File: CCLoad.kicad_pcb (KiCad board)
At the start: 2 copper layers, 100 x 50 mm, 37 parts, among them J101 BANANA, J102 BANANA, J103 MOLEX, J104 BTS117, J105 SCREW_TERMINAL, J106 MOLEX, SW101 SW_DP3T, U101 HT7533-1 (3V3), U102 CJ431, U103 MCP6002-xP

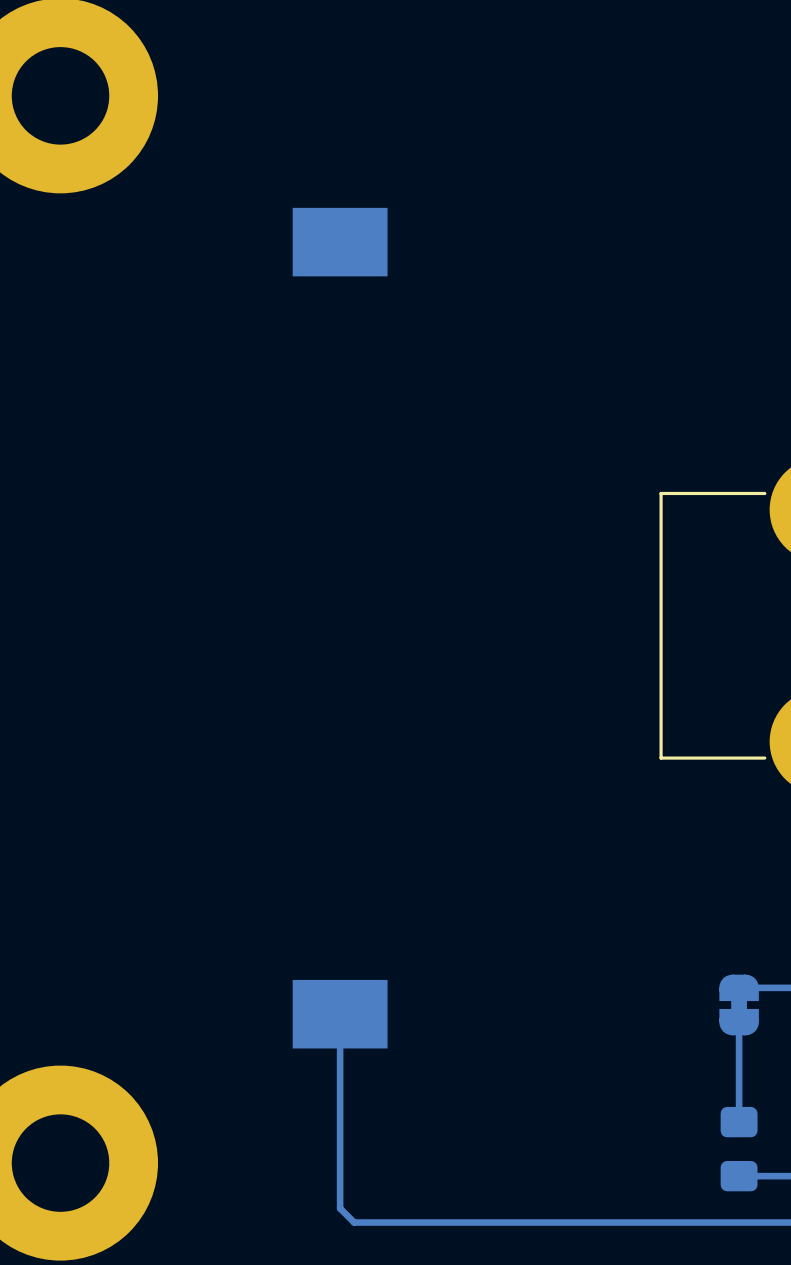
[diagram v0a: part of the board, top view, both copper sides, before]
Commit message: increases banana mounting hole to 4.5mm
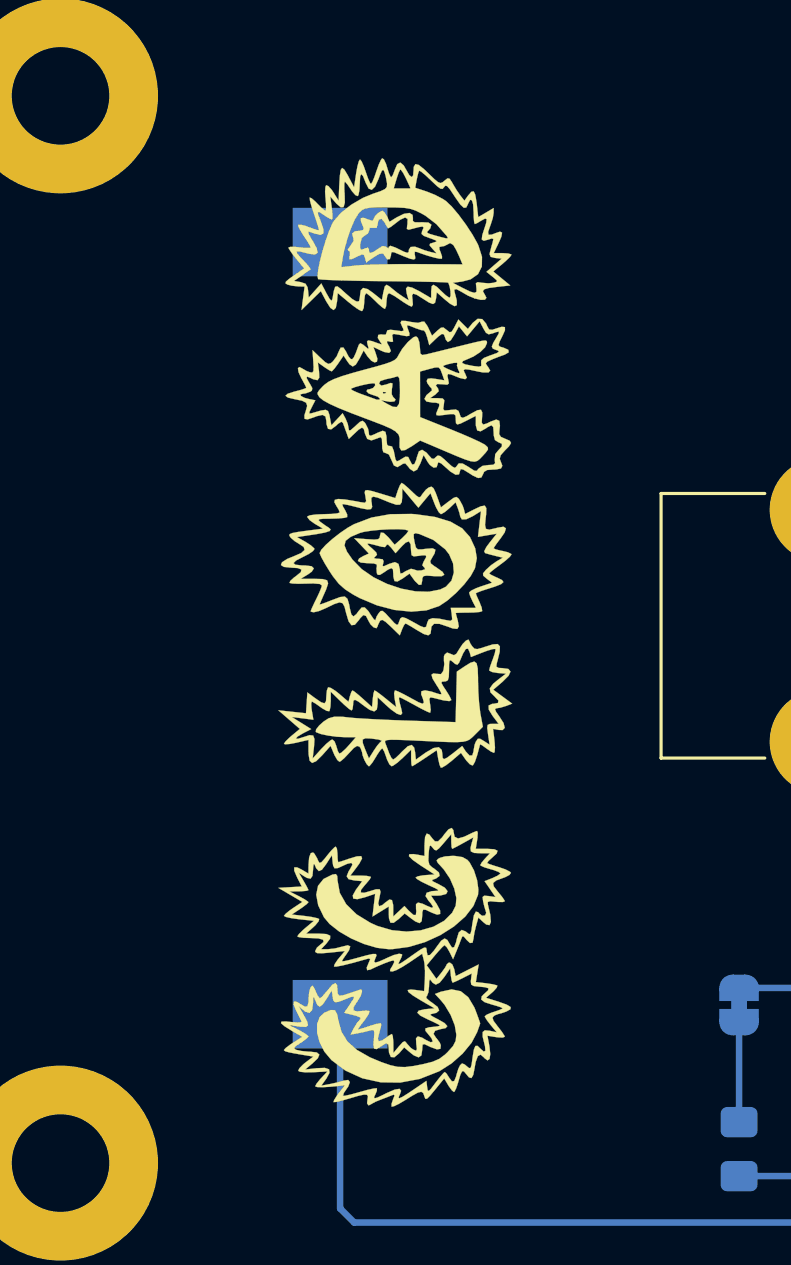
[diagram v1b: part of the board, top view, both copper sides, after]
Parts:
- added G***: LOGO, CCLoad:logo_silk, F.Cu at (118.9, 102.6)
- added G***: LOGO, CCLoad:hot_solder_mask, F.Cu at (172.3, 102.2)
